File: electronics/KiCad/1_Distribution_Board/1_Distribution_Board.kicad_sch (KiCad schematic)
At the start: 10 parts, among them J101 Conn_01x10, J102 Conn_01x06, Q101 DMG2305UX, SW101 SW_Push

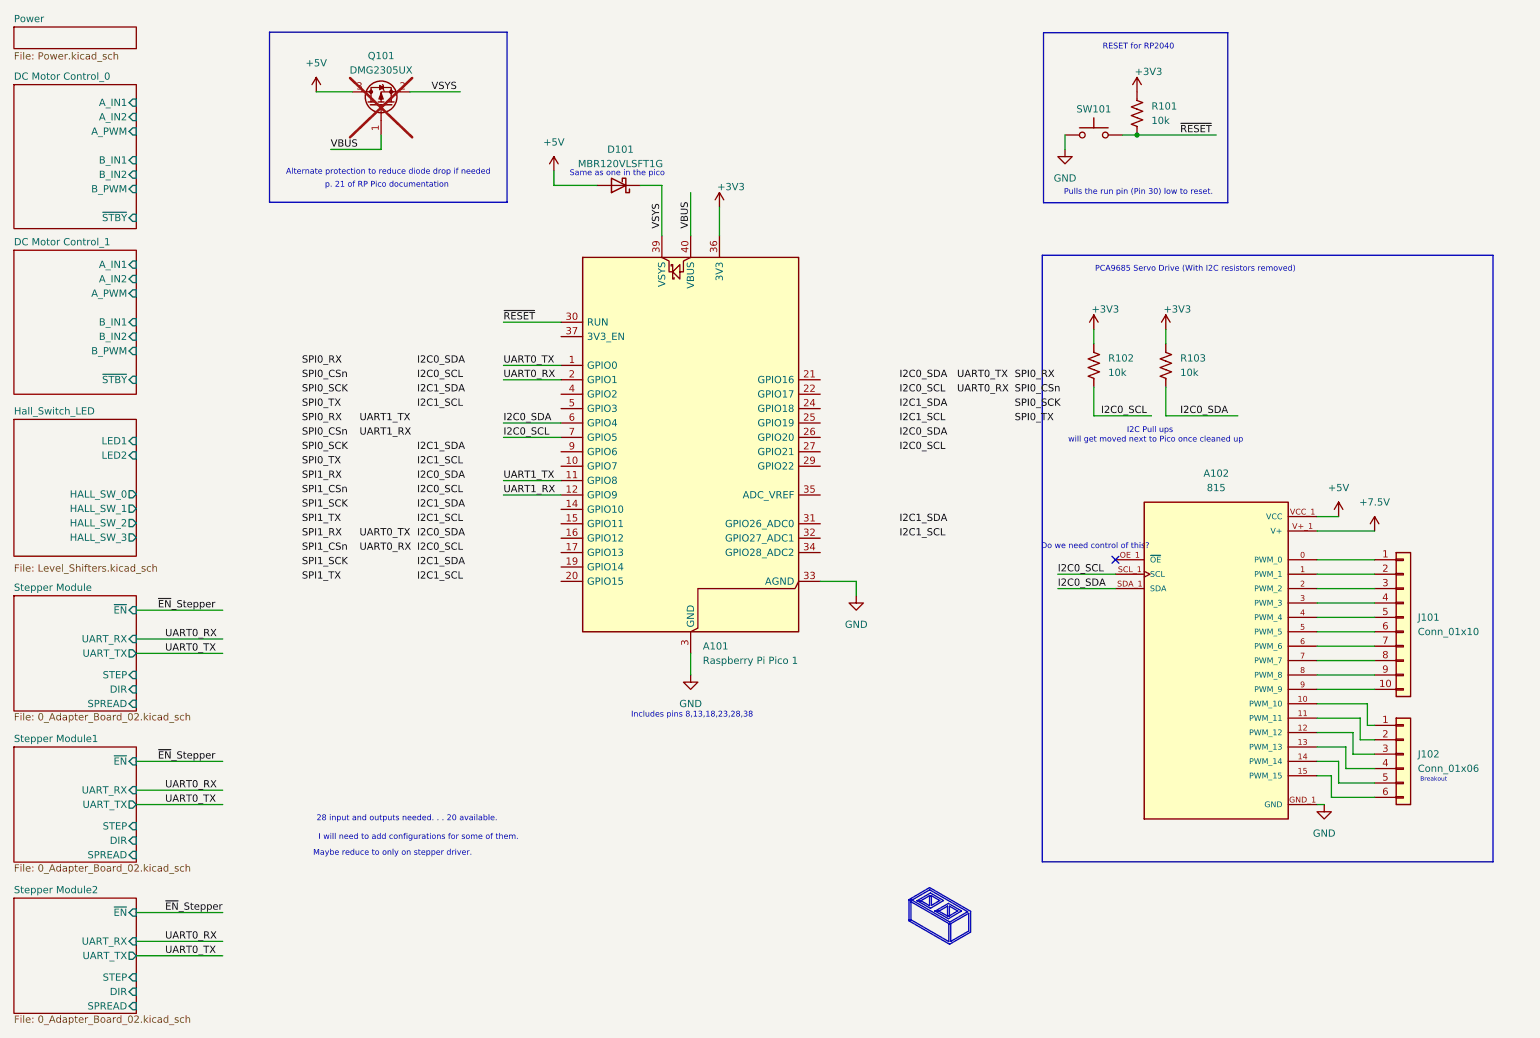
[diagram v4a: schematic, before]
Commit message: Cleaned up Power
Updated power area to include RECOM only and adding stack flex cable connector as an in-case-of
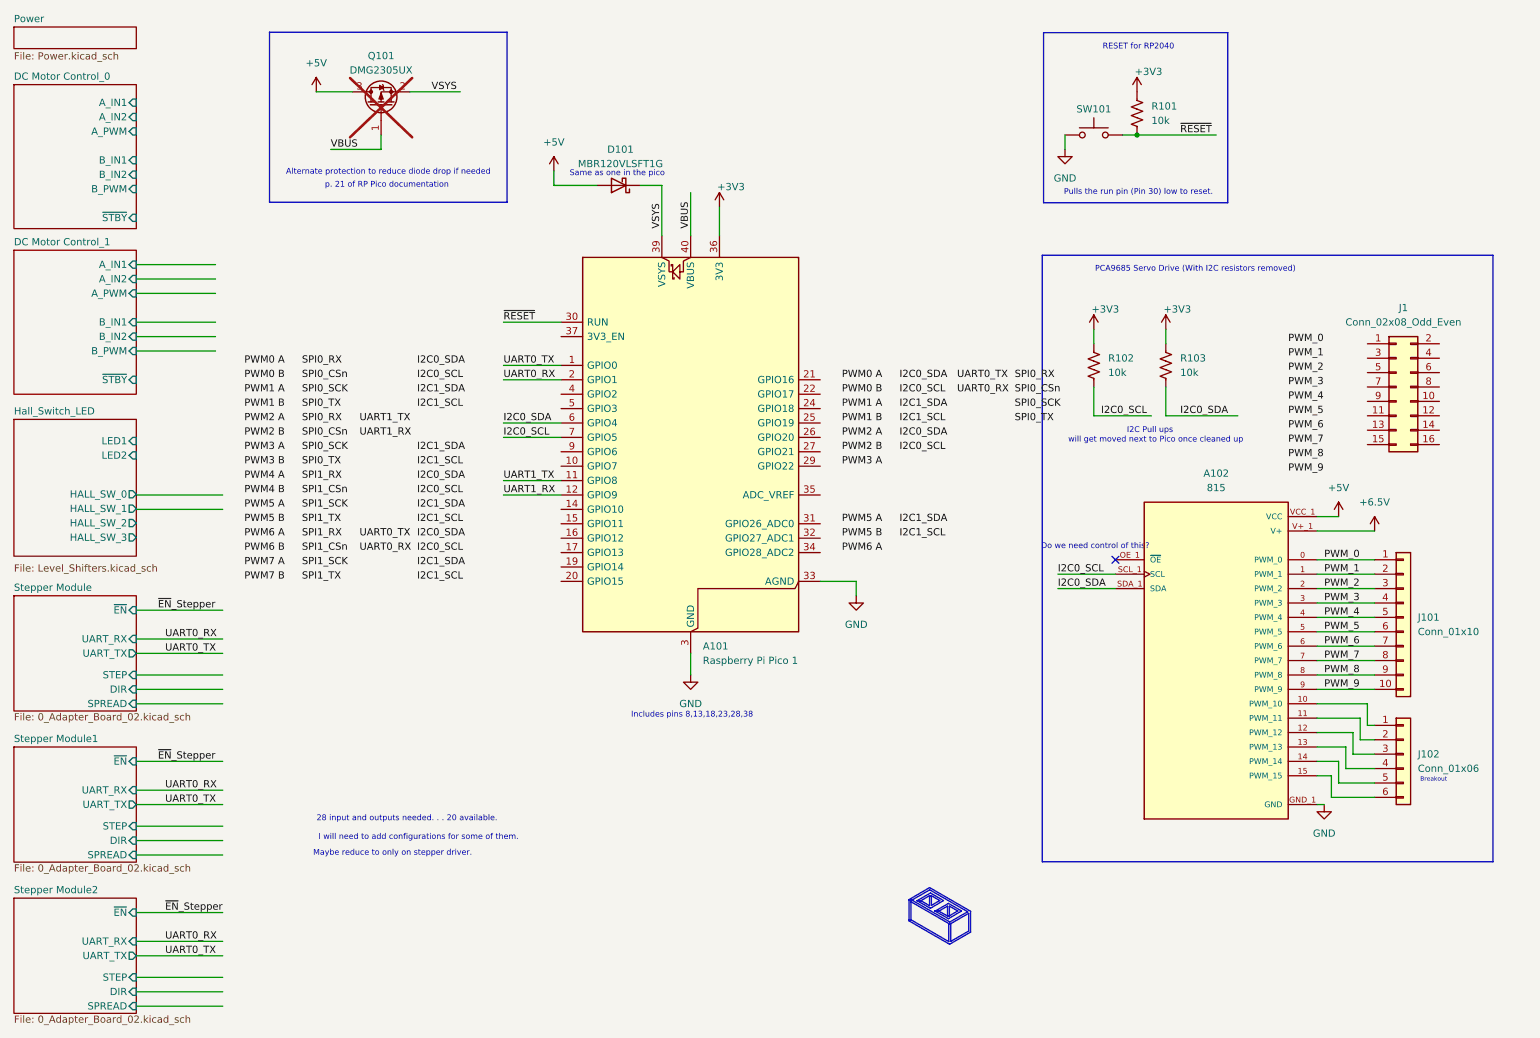
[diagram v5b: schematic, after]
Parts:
- added J1: Conn_02x08_Odd_Even, symbol Connector_Generic:Conn_02x08_Odd_Even
- SW101: footprint (none) -> Button_Switch_THT:SW_PUSH_6mm
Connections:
- net PWM_0: now reaches A102.0 (PWM_0), J101.1 (Pin_1)
- net PWM_1: now reaches A102.1 (PWM_1), J101.2 (Pin_2)
- net PWM_2: now reaches A102.2 (PWM_2), J101.3 (Pin_3)
- net PWM_3: now reaches A102.3 (PWM_3), J101.4 (Pin_4)
- net PWM_4: now reaches A102.4 (PWM_4), J101.5 (Pin_5)
- net PWM_5: now reaches A102.5 (PWM_5), J101.6 (Pin_6)
- net PWM_6: now reaches A102.6 (PWM_6), J101.7 (Pin_7)
- net PWM_7: now reaches A102.7 (PWM_7), J101.8 (Pin_8)
- net PWM_8: now reaches A102.8 (PWM_8), J101.9 (Pin_9)
- net PWM_9: now reaches A102.9 (PWM_9), J101.10 (Pin_10)
- net +7.5V renamed +6.5V

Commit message: Added 4th stepper
Added 4th stepper on SCH and PCB
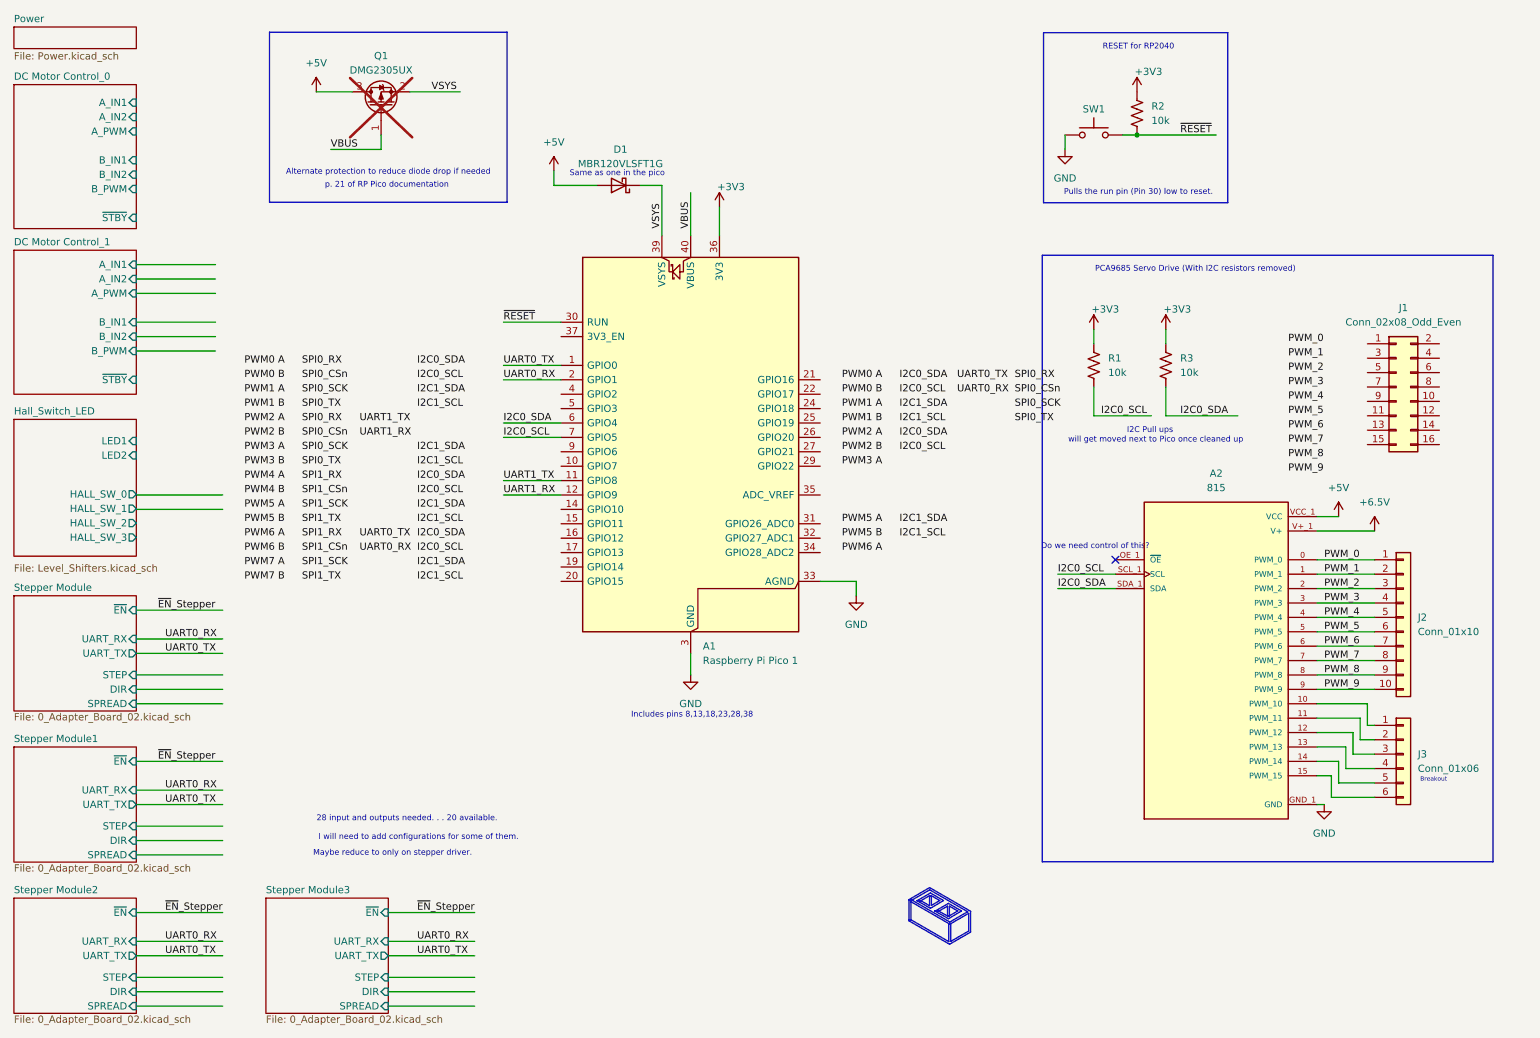
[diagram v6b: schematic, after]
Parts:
- renumbered A101 to A1, A102 to A2, D101 to D1, J101 to J2, J102 to J3, Q101 to Q1, R102 to R1, R101 to R2, R103 to R3, SW101 to SW1
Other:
- added sheet Stepper Module3 (0_Adapter_Board_02.kicad_sch)

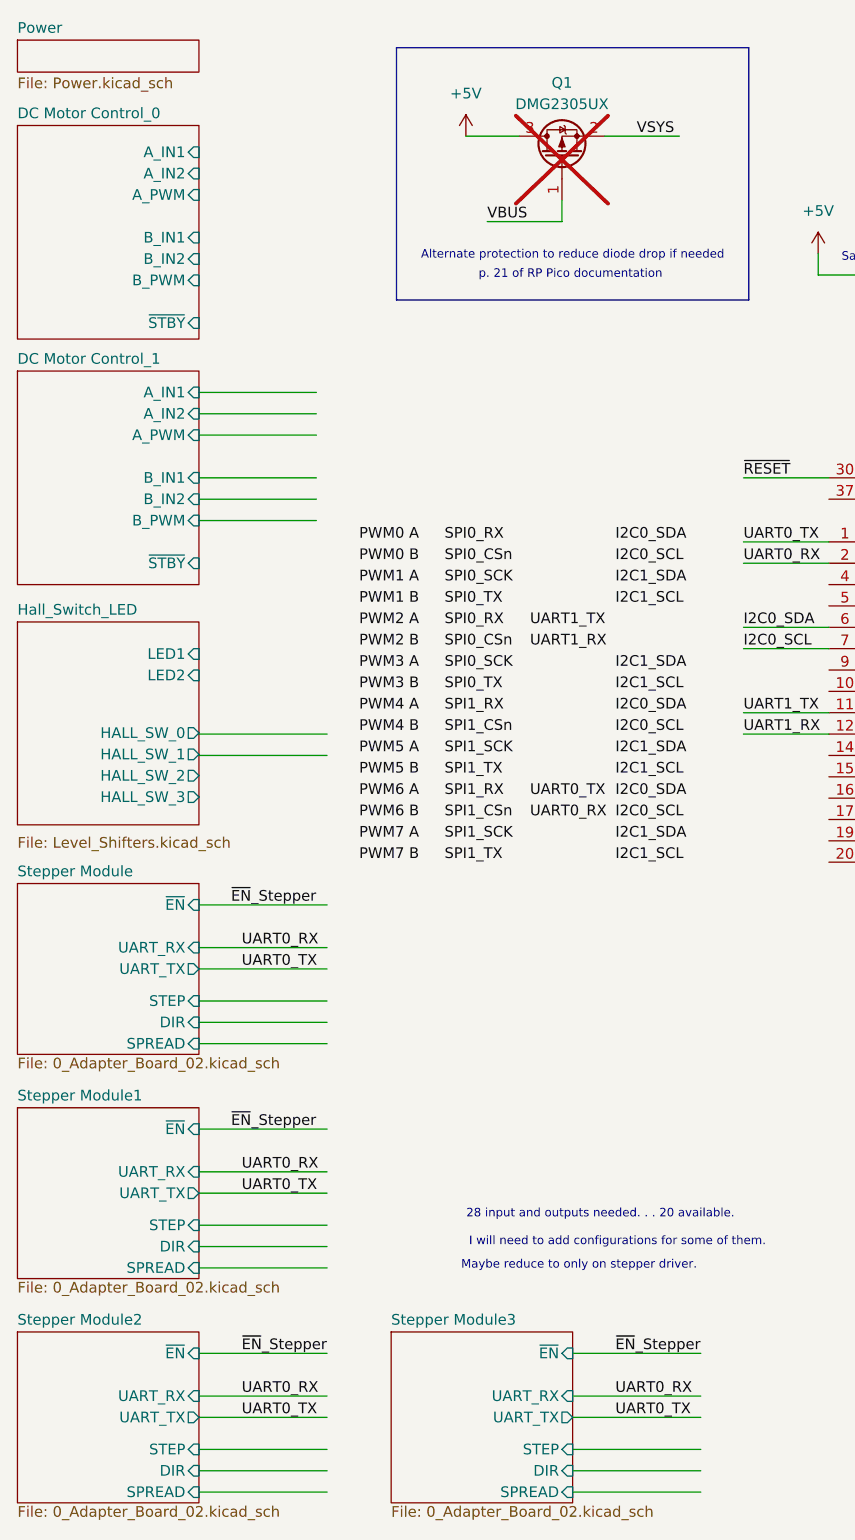
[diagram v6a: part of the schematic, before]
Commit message: Updated Schematics
Corrected Schematics to pull duplicates on the design.
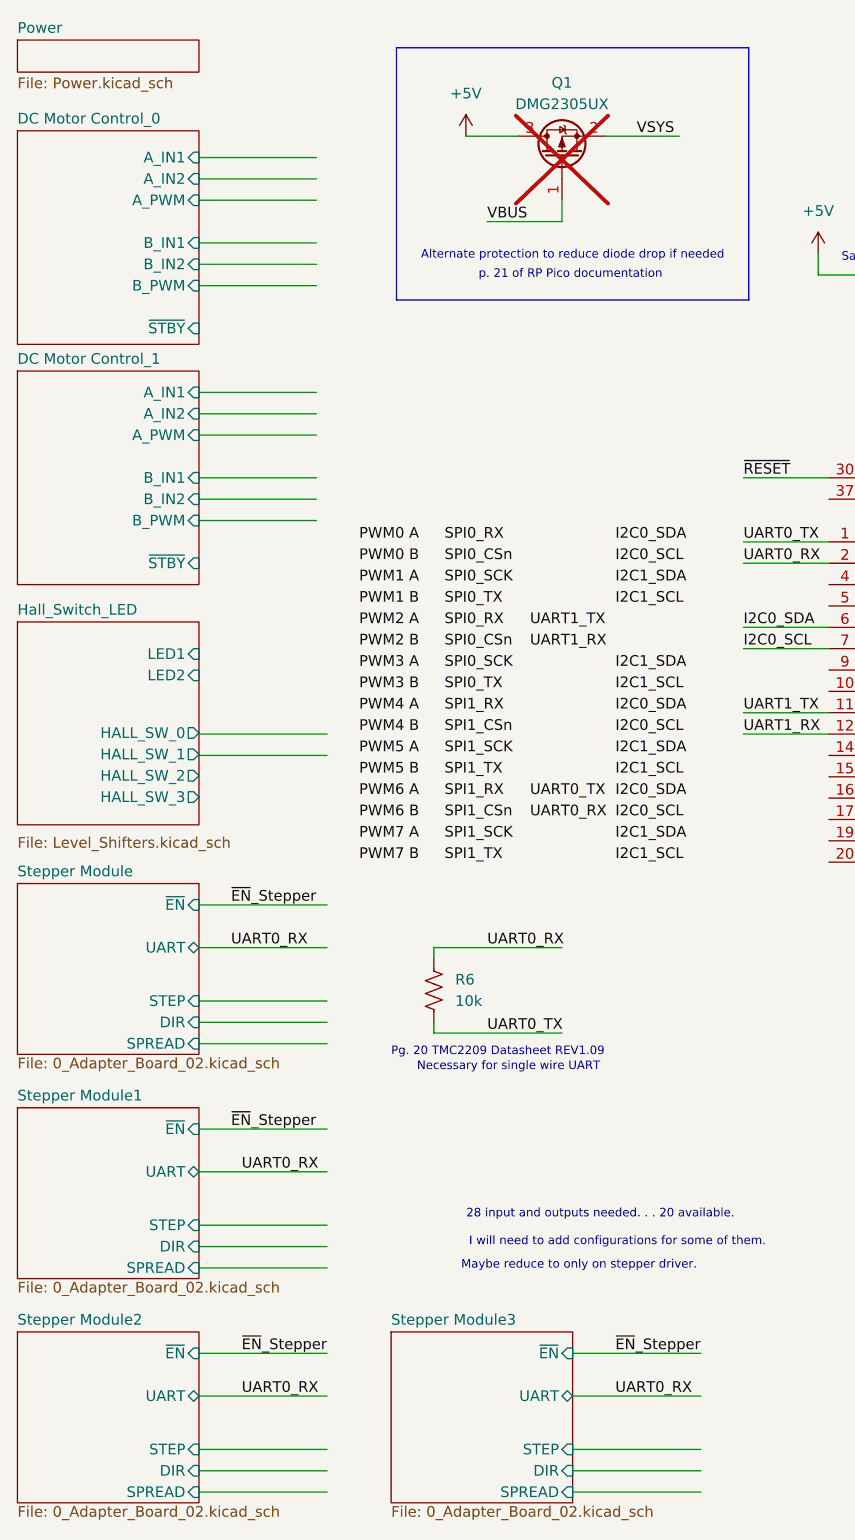
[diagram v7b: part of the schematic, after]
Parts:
- added R6: 10k, Resistor_SMD:R_0805_2012Metric_Pad1.20x1.40mm_HandSolder, symbol Device:R_US
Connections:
- net UART0_RX: now also R6.1
- net UART0_TX: now also R6.2
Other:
- sheet Stepper Module ports: added UART; removed UART_RX, UART_TX
- sheet Stepper Module1 ports: added UART; removed UART_RX, UART_TX
- sheet Stepper Module2 ports: added UART; removed UART_RX, UART_TX
- sheet Stepper Module3 ports: added UART; removed UART_RX, UART_TX
- note added: "Necessary for single wire UART"
- note added: "Pg. 20 TMC2209 Datasheet REV1.09"
